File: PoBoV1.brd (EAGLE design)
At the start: 173.4 x 70.6 mm, 89 parts, among them IC1 INA232, Q1 IPZ40N04S5L-4R8, Q2 IPZ40N04S5L-4R8, U1 TPS55288RPMR, X1 +Vin, X19 ADDRSEL, X2 BANANAJACKBANANAJACK-BLACK, X3 SDA, X4 SCL, X5 VOUT/EXT, X6 FB SEL, X7 EN SEL, X8 MODE SEL, X9 BANANAJACKBANANAJACK-RED

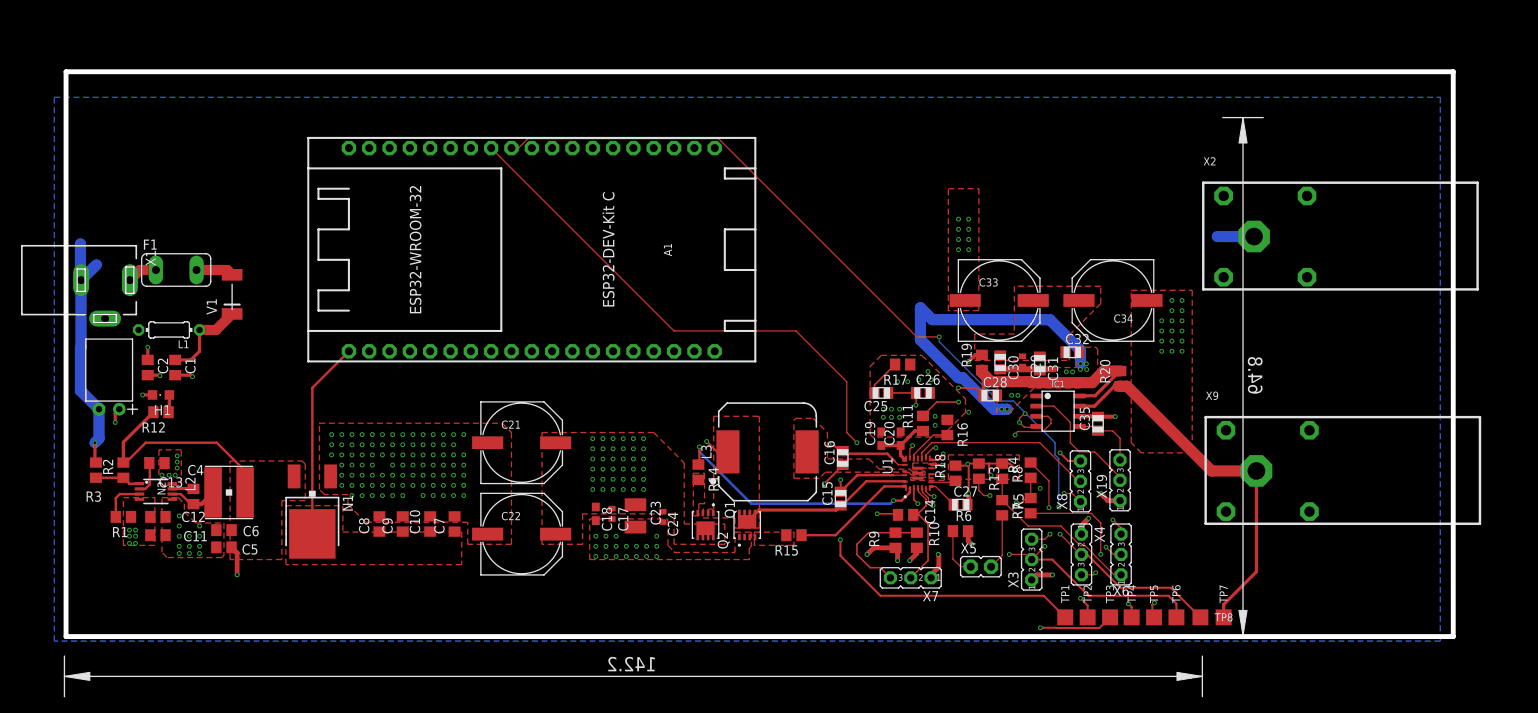
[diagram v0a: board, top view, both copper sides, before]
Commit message: Add files via upload
Final Version that includes whole layout revamp
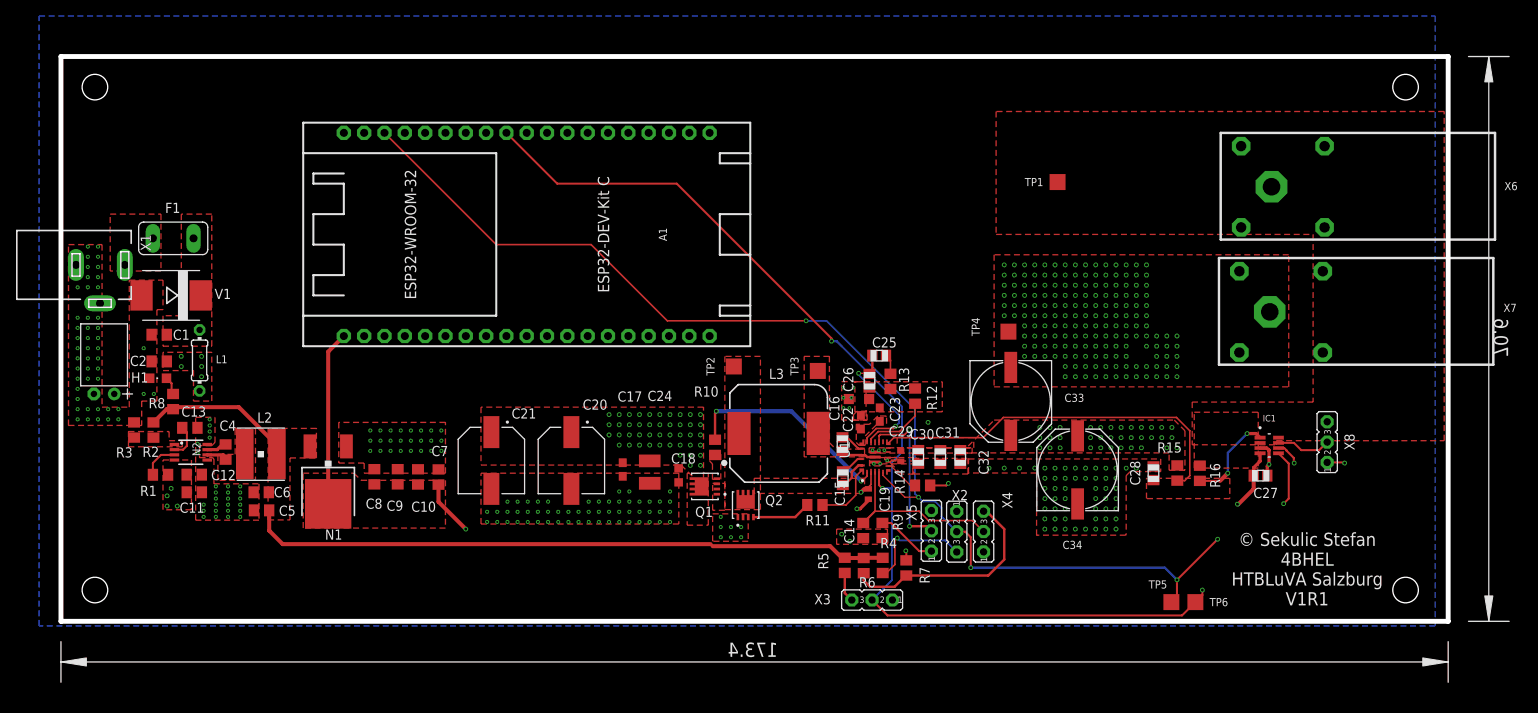
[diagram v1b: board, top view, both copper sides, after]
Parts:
- removed C35: 100n, RPoettinger:MYLIB_C0805
- removed R17: 24k9, RPoettinger:R0805
- removed R18: 50k, RPoettinger:R0805
- removed R19: 17m, RPoettinger:R0805
- removed R20: 5mR, Neo_V2.102R1:RCL_STRH_R0805
- removed TP7, TP8: TPP-SMD-20SN, testpoint:SMD-20SN
- removed X19: ADDRSEL, StefNe555:JUMPER_JP3
- removed X9: BANANAJACKBANANAJACK-RED, con_PoeD:BANANAJACK
- added ~NUDEV~1: GND-GNDA, supply-dummy:GND-GNDA
- C17: value 100n -> 4u7; device RPoettinger:MYRCL_C0402 -> RPoettinger:MYRCL_C0603
- C18: value 4u7 -> 1u; device RPoettinger:MYRCL_C0603 -> RPoettinger:MYRCL_C0603K
- C19: value 4u7 -> 100n; device RPoettinger:MYRCL_C0603 -> RPoettinger:MYRCL_C0402
- C20: value 100n -> 68u; device RPoettinger:MYRCL_C0603 -> EEHZA1H680P:CAP_EEHZA1H680P
- C21: value 100u -> 68u; device rcl_SekS_V22:PANASONIC_G -> EEHZA1H680P:CAP_EEHZA1H680P
- C22: value 100u -> 4u7; device rcl_SekS_V22:PANASONIC_G -> RPoettinger:MYRCL_C0603
- C23: value 10u -> 100n; device rcl_SekS_V22:C1210 -> RPoettinger:MYRCL_C0603
- C24: value 1u -> 10u; device rcl_SekS_V22:C0402 -> rcl_SekS_V22:C1210
- C27: value 8n2 -> 100n
- F1: value 4A -> 7A
- IC1: device FaBo-Sensor:TI-INA219 -> INA232AIDDFR:SOT65P280X110-8N
- R10: value 115k -> 1R; device rcl_STRH:R0805 -> RPoettinger:R0805
- R11: value 100k -> 1R; device rcl_STRH:R0805 -> RPoettinger:R0805
- R12: value 330R -> 34k8; device rcl_STRH:R0805 -> RPoettinger:R0805
- R13: value 14k3 -> 24k9; device rcl_STRH:R0805 -> RPoettinger:R0805
- R14: value 1R -> 50k
- R15: value 1R -> 17m
- R16: value 34k8 -> 5mR; device RPoettinger:R0805 -> Neo_V2.102R1:RCL_STRH_R0805
- R6: value 50R -> 147k
- R7: value 100k -> 115k
- R8: value 11.3k -> 330R
- R9: value 147k -> 14k3
- V1: value SM4001 -> B560C-13-F; device diode_STRH:SOD87 -> B560C-13-F:SMC
- X2: value BANANAJACKBANANAJACK-BLACK -> SDA; device con_PoeD:BANANAJACK -> RPoettinger:JUMPER_JP3
- X3: value SDA -> SCL
- X4: value SCL -> EN SEL
- X5: value VOUT/EXT -> MODE SEL; device Neo_V2.102R1:JUMPER_STRH_JP1 -> RPoettinger:JUMPER_JP3
- X6: value FB SEL -> RED; device RPoettinger:JUMPER_JP3 -> con_PoeD:BANANAJACK
- X7: value EN SEL -> BLACK; device RPoettinger:JUMPER_JP3 -> con_PoeD:BANANAJACK
- X8: value MODE SEL -> ADDRSEL; device RPoettinger:JUMPER_JP3 -> StefNe555:JUMPER_JP3
- moved R8 104.0 mm to (13.6, 29.3)
- moved R12 94.3 mm to (106.3, 30.0), turned to 270 degrees
- moved X7 55.8 mm to (150.7, 40.5), turned to 0 degrees
- moved TP1 54.4 mm to (124.1, 56.7), turned to 180 degrees
- moved TP2 54.2 mm to (83.7, 33.7)
- moved X2 52.4 mm to (111.5, 13.0), turned to 270 degrees
- moved X6 49.7 mm to (150.9, 56.1), turned to 0 degrees
- moved R15 48.5 mm to (139.1, 20.3), turned to 90 degrees
- moved TP3 47.8 mm to (94.2, 33.1)
- moved C22 44.7 mm to (99.6, 26.7), turned to 90 degrees
- moved C20 41.2 mm to (63.4, 21.9), turned to 270 degrees
- moved TP4 38.9 mm to (118.0, 38.0)
- moved C27 37.7 mm to (149.5, 20.0)
- moved C23 33.1 mm to (101.9, 27.6), turned to 90 degrees
- moved R16 32.1 mm to (141.9, 20.3)
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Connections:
- removed net GND: A1.GND, A1.GND@1, A1.GND@2, C14.2, C19.2, C20.2, C26.2, C27.2, C35.2, IC1.6, R10.1, R13.1, R16.1, R17.1, R18.2, R8.1, U1.10, U1.24, U1.9, X19.1, X3.1, X4.1, X7.1, X8.3
- removed net N$11: R7.2, X5.2
- removed net N$16: R6.1, X5.1
- removed net N$22: F1.2, V1.A
- removed net N$4: R11.2, X6.3
- removed net N$6: C27.1, U1.7
- removed net N$8: R7.1, R8.2, X6.1
- net +3.3: now also C27.1, IC1.4
- net +3.3V: now also X8.3; no longer C35.1, IC1.5, X19.3
- net +5V: now also R6.2, R8.2; no longer R12.2, R9.2
- net +V: now also C22.1, C23.1; no longer C19.1, C20.1, R11.1
- net ADDRSEL: now also IC1.7, X8.2; no longer IC1.2, X19.2
- net BOOT1: no longer TP1.TP
- net BOOT2: no longer TP2.TP
- net DR1H: now also R10.1; no longer R14.1
- net DR1L: now also R11.1; no longer R15.1
- net EN: now also X4.2; no longer X7.2
- net FB: no longer X6.2
- net ISN: now also IC1.1, R15.1, R16.2; no longer IC1.8, R19.1, R20.2
- net ISP: now also R15.2; no longer R19.2
- net MODE: now also X5.2; no longer X8.2
- net N$10: now also X3.3; no longer X4.3
- net N$12: now also R13.2; no longer R17.2
- net N$14: now also R14.1; no longer R18.1
- net N$15: now also R12.2; no longer R16.2
- net N$17: now also R8.1; no longer R12.1
- net N$18: now also R9.2, X5.1; no longer R13.2, X8.1
- net N$20: now also F1.2, V1.C; no longer V1.K
- net N$3: now also R10.2; no longer R14.2
- net N$5: now also R11.2; no longer R15.2
- net N$7: now also R6.1, R7.2, X4.3; no longer R10.2, R9.1, X7.3
- net N$9: now also X2.3; no longer X3.3
- net PGND: now also A1.GND, A1.GND@1, A1.GND@2, C14.2, C19.2, C20.2, C21.2, C22.2, C26.2, C27.2, IC1.3, R12.1, R13.1, R14.2, R7.1, R9.1, TP4.TP, U1.10, U1.24, U1.9, V1.A, X2.1, X3.1, X4.1, X5.3, X7.P$1, X8.1, ~NUDEV~1.GND, ~NUDEV~1.PGND; no longer C21.-, C22.-, TP5.TP, X2.P$1
- net SCL: now also IC1.5, TP6.TP, X3.2; no longer IC1.4, TP8.TP, X4.2
- net SDA: now also A1.GPIO22, IC1.6, TP5.TP, X2.2; no longer A1.GPIO19, IC1.3, TP6.TP, X3.2
- net SW1: now also TP2.TP; no longer TP3.TP
- net SW2: now also TP3.TP; no longer TP4.TP
- net VCC: now also C19.1, C20.1, C21.1; no longer C21.+, C22.+, C23.1, R6.2
- net VOUT: now also IC1.2, R16.1, TP1.TP, X6.P$1; no longer IC1.7, R20.1, TP7.TP, X9.P$1
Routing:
- net +3.3: track 24.7 -> 140.5 mm, vias 0 -> 2
- net SW1: track 93.6 -> 3.85 mm, vias 2 -> 0
- net PGND: track 92.1 -> 12.6 mm, vias 165 -> 402
- net BOOT2: track 60.3 -> 3.04 mm, vias 2 -> 0
- net SW2: track 54.7 -> 4.38 mm, vias 2 -> 0
- net BOOT1: track 51.1 -> 3.02 mm, vias 2 -> 0
- net VOUT: track 47.5 -> 0.00 mm
- net +5V: track 140.0 -> 100.0 mm, vias 4 -> 0
- net GND: track 38.0 -> 0.00 mm, vias 26 -> 0
- net N$4: track 32.8 -> 0.00 mm, vias 2 -> 0
- net FB: track 30.7 -> 0.00 mm, vias 2 -> 0
- net SDA: track 141.9 -> 164.1 mm
- net N$8: track 21.4 -> 0.00 mm
- net VCC: track 7.47 -> 26.8 mm, vias 46 -> 54
- net ISP: track 17.8 -> 0.00 mm, vias 3 -> 39
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- added copper zone on layer 1, net +V
- added copper zone on layer 1, net ISN
- added copper zone on layer 15, net ISP
- added copper zone on layer 1, net N$1
- added copper zone on layer 1, net N$20
- added copper zone on layer 1, net N$29
- added copper zone on layer 1, net N$31
- added copper zone on layer 15, net PGND
- added copper zone on layer 2, net PGND
- added copper zone on layer 1, net VOUT
- removed copper zone on layer 1, net GND
- removed copper zone on layer 2, net GND
- removed copper zone on layer 1, net N$5
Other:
- board text added: "© Sekulic Stefan 4BHEL HTBLuVA Salzburg V1R1"
- board text removed: "BOOT1"
- board text removed: "BOOT2"
- board text removed: "PGND"
- board text removed: "SW1"
